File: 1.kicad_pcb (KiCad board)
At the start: 2 copper layers, 88.9 x 48.3 mm, 44 parts, among them J1 Micro_SD_Card, J10 I2C1, J11 I2C2, J12 B3..9A, J2 USB_B_Micro, J3 Conn_Power, J4 SWD, J5 Protected, J6 SPI1, J7 ADC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

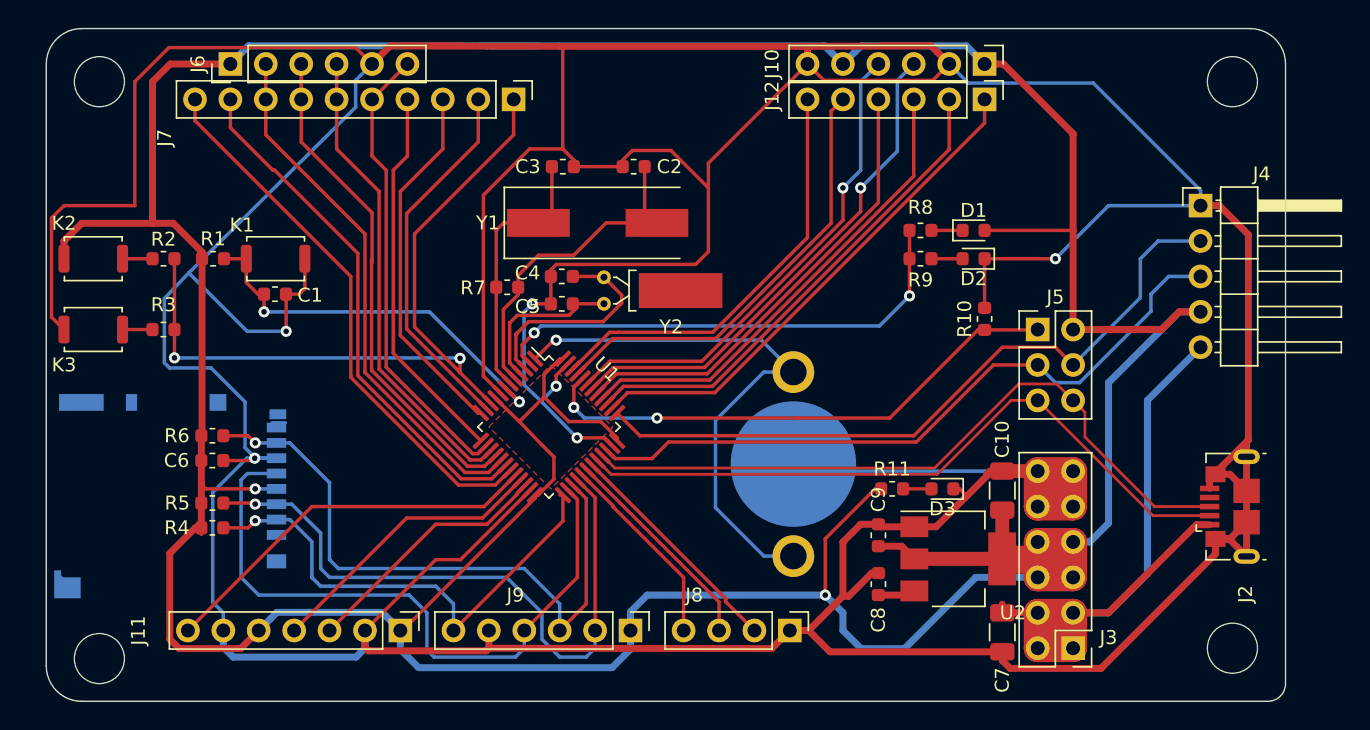
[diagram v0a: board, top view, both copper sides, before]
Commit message: move U1(STM32 Chip)
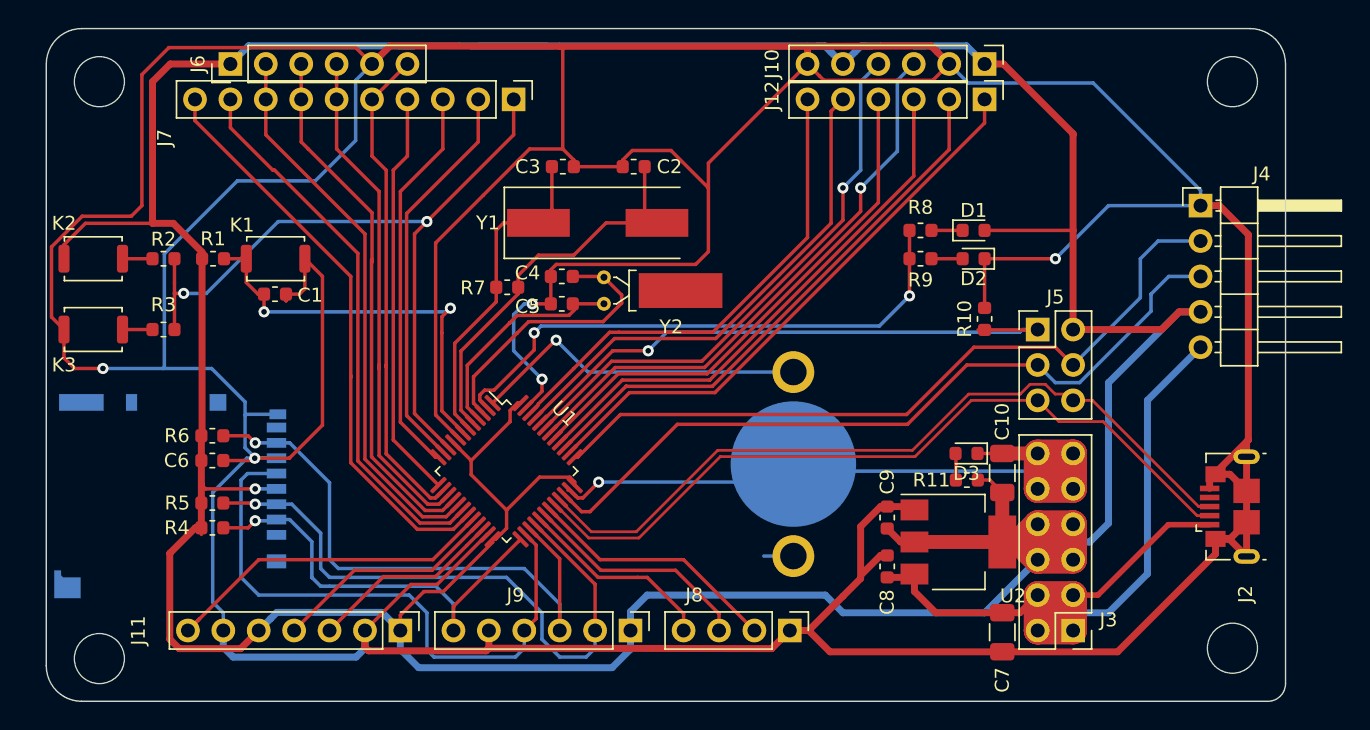
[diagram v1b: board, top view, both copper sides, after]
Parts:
- moved R11 5.40 mm to (162.6, 118.7), turned to 180 degrees
- moved U1 4.40 mm to (129.5, 118.1)
- moved D3 3.07 mm to (162.5, 116.8)
- moved C8 1.42 mm to (156.8, 124.9)
- moved C9 1.42 mm to (156.8, 121.4)
- moved J3 1.27 mm to (170.2, 129.5)
- moved C10 1.26 mm to (165.1, 118.2)
- moved U2 1.21 mm to (161.9, 123.2)
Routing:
- net GND: track 506.2 -> 528.3 mm
- net Net-(BT1-Pad1): track 40.3 -> 26.7 mm
- net +3V3: track 329.4 -> 316.5 mm, vias 2 -> 1
- net +5V: track 57.3 -> 63.4 mm
- net /USB_D-: track 50.0 -> 55.5 mm
- net /SD_SCLK: track 48.2 -> 43.1 mm
- net /RG_LED: track 35.6 -> 40.4 mm
- net /SWDIO: track 50.0 -> 54.8 mm
- net /SD_CS: track 37.3 -> 32.6 mm
- net /USB_D+: track 51.2 -> 55.6 mm
- net /OSC_8M1: track 24.1 -> 28.5 mm
- net /PB3: track 36.9 -> 41.4 mm
- net /PB9: track 30.6 -> 35.0 mm
- net /OSC_32K1: track 15.9 -> 20.3 mm
- net /PB11: track 18.4 -> 14.0 mm
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- removed copper zone on F.Cu, net +3V3

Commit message: move edge
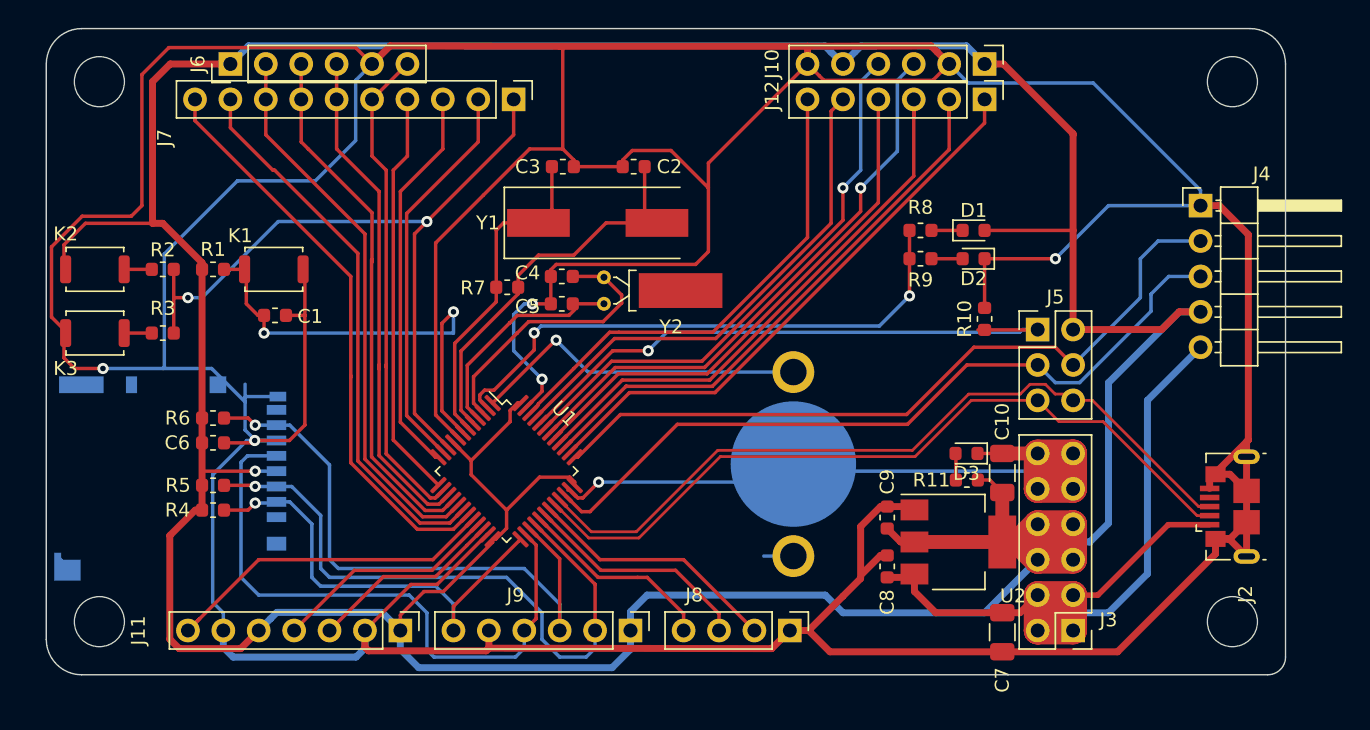
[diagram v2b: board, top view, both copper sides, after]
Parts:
- moved C1 1.52 mm to (112.9, 106.9)
- moved R4 1.27 mm to (108.5, 120.9)
- moved C6 1.27 mm to (108.5, 116.1)
- moved R5 1.27 mm to (108.5, 119.1)
- moved R6 1.27 mm to (108.5, 114.3)
- moved J1 1.27 mm to (105.4, 118.6)
- moved K1 0.77 mm to (112.8, 103.6)
- moved K2 0.77 mm to (100.0, 103.6)
- moved R2 0.76 mm to (104.9, 103.6)
- moved R1 0.76 mm to (108.5, 103.6)
- moved K3 0.28 mm to (100.0, 108.2)
- moved R3 0.26 mm to (104.9, 108.2)
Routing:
- net GND: track 528.3 -> 525.5 mm
- net +3V3: track 316.5 -> 315.1 mm
- net /NRST: track 29.5 -> 30.8 mm
- net /SD_SCLK: track 43.1 -> 44.3 mm
- net /SD_DO: track 42.4 -> 43.7 mm
- net /SD_DI: track 45.2 -> 46.4 mm
- net /SD_CS: track 32.6 -> 33.8 mm
- net /PA0: track 55.8 -> 55.0 mm
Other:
- board size 88.9 x 48.3 mm -> 88.9 x 46.4 mm
- board text added: "ADC CH9..0"
- board text added: "SWD"
- board text added: "USB"

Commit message: movdify some line
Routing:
- net /NRST: track 30.8 -> 30.1 mm
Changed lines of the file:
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@@
     (thickness 1.6)
     (drawings 27)
-    (tracks 664)
+    (tracks 665)
     (zones 0)
     (modules 44)
@@
   (segment (start 110.998 120.904) (end 111.506 120.396) (width 0.25) (layer F.Cu) (net 4))
   (segment (start 109.271 120.904) (end 110.998 120.904) (width 0.25) (layer F.Cu) (net 4))
-  (segment (start 112.141 108.204) (end 112.141 108.204) (width 0.25) (layer F.Cu) (net 5))
-  (via (at 125.73 106.68) (size 0.8) (drill 0.4) (layers F.Cu B.Cu) (net 5))
-  (segment (start 112.141 108.204) (end 112.141 108.204) (width 0.25) (layer F.Cu) (net 5))
-  (via (at 112.141 108.204) (size 0.8) (drill 0.4) (layers F.Cu B.Cu) (net 5))
-  (segment (start 126.419891 115.308103) (end 126.419891 115.343445) (width 0.25) (layer F.Cu) (net 5))
-  (segment (start 124.900666 113.788878) (end 126.419891 115.308103) (width 0.25) (layer F.Cu) (net 5))
-  (segment (start 125.73 106.68) (end 124.900666 107.509334) (width 0.25) (layer F.Cu) (net 5))
-  (segment (start 124.900666 107.509334) (end 124.900666 113.788878) (width 0.25) (layer F.Cu) (net 5))
-  (segment (start 112.141 108.204) (end 125.73 108.204) (width 0.25) (layer B.Cu) (net 5))
-  (segment (start 112.141 106.934) (end 112.141 108.204) (width 0.25) (layer F.Cu) (net 5))
   (segment (start 111.7035 106.934) (end 112.141 106.934) (width 0.25) (layer F.Cu) (net 5))
+  (segment (start 110.871 106.1015) (end 110.871 106.1015) (width 0.25) (layer F.Cu) (net 5))
+  (segment (start 110.871 104.394) (end 110.871 106.1015) (width 0.25) (layer F.Cu) (net 5))
+  (segment (start 109.271 103.632) (end 110.744 103.632) (width 0.25) (layer F.Cu) (net 5))
   (segment (start 110.871 106.1015) (end 111.7035 106.934) (width 0.25) (layer F.Cu) (net 5))
-  (segment (start 110.871 104.394) (end 110.871 106.1015) (width 0.25) (layer F.Cu) (net 5))
-  (segment (start 125.73 106.68) (end 125.73 108.204) (width 0.25) (layer B.Cu) (net 5))
-  (segment (start 109.271 103.632) (end 110.744 103.632) (width 0.25) (layer F.Cu) (net 5))
+  (via (at 110.871 106.1015) (size 0.8) (drill 0.4) (layers F.Cu B.Cu) (net 5))
+  (segment (start 110.871 106.1015) (end 125.4055 106.1015) (width 0.25) (layer B.Cu) (net 5))
+  (segment (start 125.4055 106.1015) (end 125.9135 106.1015) (width 0.25) (layer B.Cu) (net 5))
+  (segment (start 125.9135 106.1015) (end 125.9135 106.1015) (width 0.25) (layer B.Cu) (net 5))
+  (via (at 125.9135 106.1015) (size 0.8) (drill 0.4) (layers F.Cu B.Cu) (net 5))
+  (segment (start 124.900666 107.114334) (end 125.9135 106.1015) (width 0.25) (layer F.Cu) (net 5))
+  (segment (start 124.900666 113.788878) (end 124.900666 107.114334) (width 0.25) (layer F.Cu) (net 5))
+  (segment (start 126.419891 115.308103) (end 124.900666 113.788878) (width 0.25) (layer F.Cu) (net 5))
+  (segment (start 126.419891 115.343445) (end 126.419891 115.308103) (width 0.25) (layer F.Cu) (net 5))
   (segment (start 133.934717 119.469322) (end 133.970057 119.469322) (width 0.25) (layer F.Cu) (net 7))
   (segment (start 132.863822 104.194178) (end 132.8545 104.2035) (width 0.25) (layer F.Cu) (net 7))
@@
   (segment (start 170.18 93.9) (end 170.18 93.98) (width 0.5) (layer F.Cu) (net 8))
   (segment (start 163.83 88.9) (end 165.18 88.9) (width 0.5) (layer F.Cu) (net 8))
-  (segment (start 111.506 118.11) (end 107.95 118.11) (width 0.25) (layer F.Cu) (net 8))
   (segment (start 109.728 88.9) (end 105.41 88.9) (width 0.5) (layer F.Cu) (net 8))
   (segment (start 105.41 88.9) (end 104.14 90.17) (width 0.5) (layer F.Cu) (net 8))
@@
   (segment (start 99.33 100.33) (end 104.14 100.33) (width 0.25) (layer F.Cu) (net 8))
   (segment (start 97.79 101.87) (end 99.33 100.33) (width 0.25) (layer F.Cu) (net 8))
-  (segment (start 107.696 120.904) (end 107.696 116.078) (width 0.5) (layer F.Cu) (net 8))
   (segment (start 107.696 116.078) (end 107.696 114.3) (width 0.5) (layer F.Cu) (net 8))
   (segment (start 107.696 103.632) (end 107.696 114.3) (width 0.5) (layer F.Cu) (net 8))
@@
   (segment (start 107.696 103.157) (end 104.869 100.33) (width 0.5) (layer F.Cu) (net 8))
   (segment (start 107.696 103.632) (end 107.696 103.157) (width 0.5) (layer F.Cu) (net 8))
+  (segment (start 107.95 118.11) (end 107.696 117.856) (width 0.25) (layer F.Cu) (net 8))
+  (segment (start 111.506 118.11) (end 107.95 118.11) (width 0.25) (layer F.Cu) (net 8))
+  (segment (start 107.696 117.856) (end 107.696 116.078) (width 0.5) (layer F.Cu) (net 8))
+  (segment (start 107.696 120.904) (end 107.696 117.856) (width 0.5) (layer F.Cu) (net 8))
   (segment (start 170.25 129.64) (end 170.18 129.71) (width 0.25) (layer F.Cu) (net 10))
   (segment (start 179.324 109.22) (end 175.514 113.03) (width 0.5) (layer B.Cu) (net 10))

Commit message: gnd line
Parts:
- moved R7 0.82 mm to (128.8, 105.2)
- moved Y2 0.80 mm to (135.7, 106.1)
- moved C4 0.69 mm to (132.8, 104.1)
- moved C5 0.69 mm to (132.8, 106.1)
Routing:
- net GND: track 525.5 -> 545.1 mm
- net /OSC_32K2: track 16.1 -> 15.2 mm
- net /OSC_8M2: track 23.5 -> 24.3 mm
- net /RG_LED: track 40.4 -> 39.6 mm
- net /OSC_32K1: track 20.3 -> 19.8 mm

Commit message: op lines
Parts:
- moved J4 3.81 mm to (175.5, 99.1)
- moved J2 3.81 mm to (177.6, 120.7)
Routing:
- net +3V3: track 315.4 -> 289.7 mm
- net GND: track 545.1 -> 526.4 mm
- net +5V: track 63.4 -> 57.4 mm
- net /SWDCLK: track 54.0 -> 51.4 mm
- net /SWDIO: track 54.8 -> 52.7 mm
- net /USB_D+: track 55.6 -> 54.6 mm
- net /USB_D-: track 55.5 -> 54.9 mm
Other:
- board size 88.9 x 46.4 mm -> 86.4 x 46.4 mm

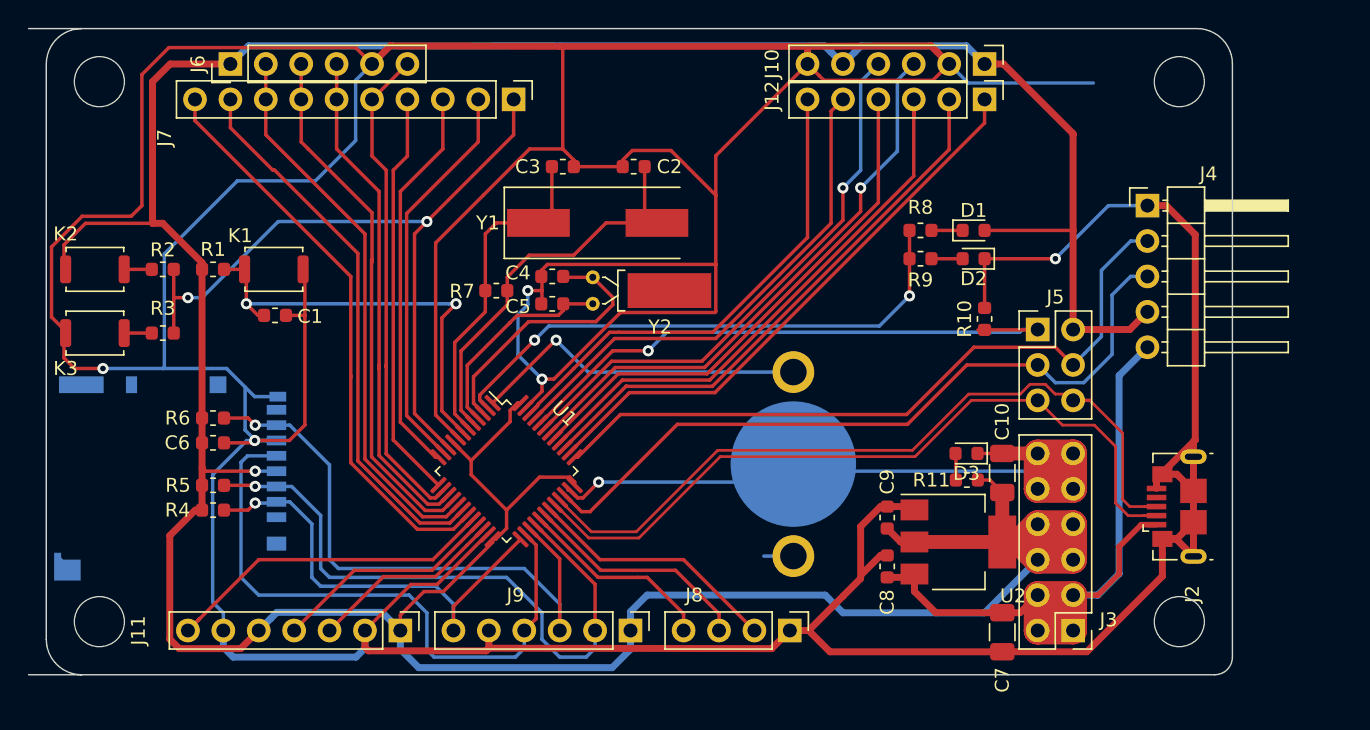
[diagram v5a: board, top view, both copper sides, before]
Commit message: resize edge
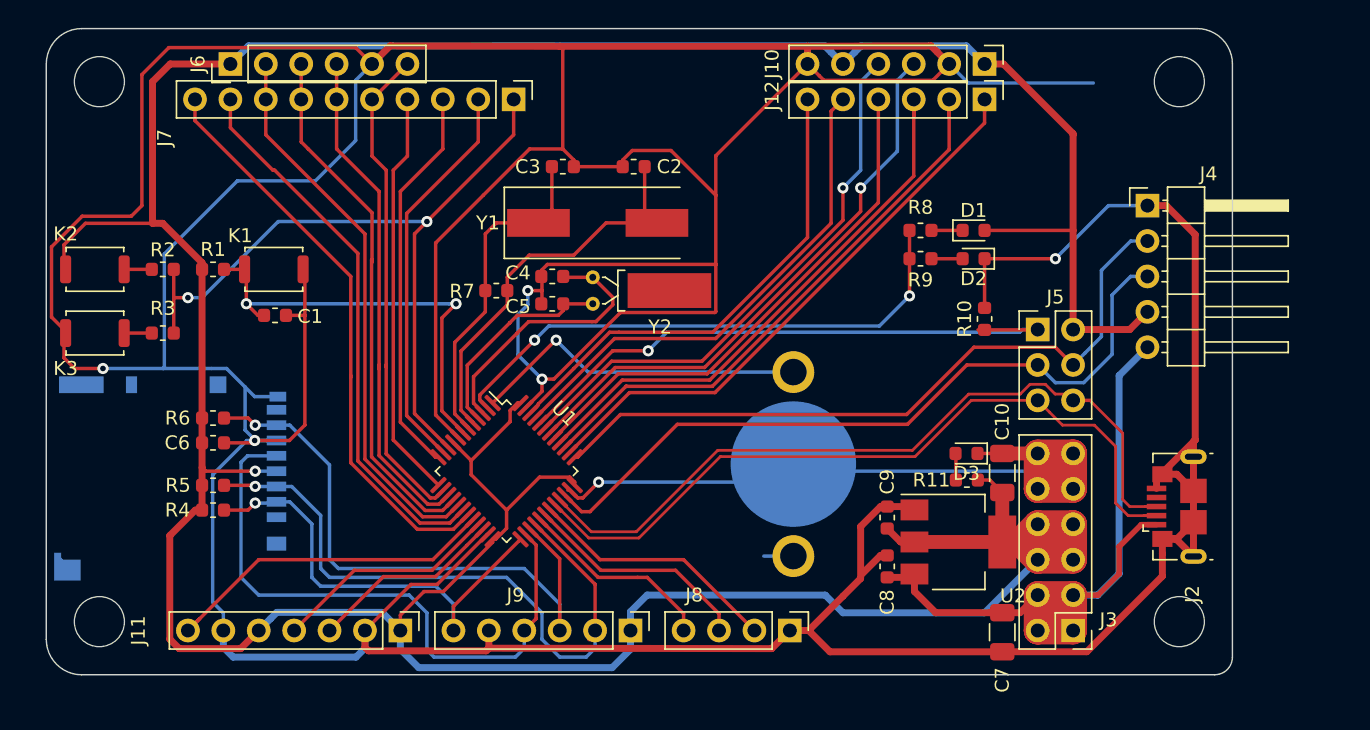
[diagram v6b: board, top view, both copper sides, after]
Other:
- board size 86.4 x 46.4 mm -> 85.1 x 46.4 mm
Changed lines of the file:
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@@
   (gr_arc (start 99.06 88.9) (end 99.06 86.36) (angle -90) (layer Edge.Cuts) (width 0.1))
   (gr_line (start 181.61 88.9) (end 181.61 131.445) (layer Edge.Cuts) (width 0.1))
-  (gr_line (start 95.25 86.36) (end 179.07 86.36) (layer Edge.Cuts) (width 0.1))
+  (gr_line (start 99.06 86.36) (end 179.07 86.36) (layer Edge.Cuts) (width 0.1))
   (gr_line (start 96.52 130.175) (end 96.52 88.9) (layer Edge.Cuts) (width 0.1))
-  (gr_line (start 180.34 132.715) (end 95.25 132.715) (layer Edge.Cuts) (width 0.1))
+  (gr_line (start 180.34 132.715) (end 99.06 132.715) (layer Edge.Cuts) (width 0.1))
   (gr_text "MCO Tx Rx GND" (at 146.05 132.08) (layer Dwgs.User)
     (effects (font (size 0.9 0.9) (thickness 0.15)))

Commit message: op gnd line
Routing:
- net GND: track 526.4 -> 535.6 mm
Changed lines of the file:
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@@
     (thickness 1.6)
     (drawings 27)
-    (tracks 672)
+    (tracks 674)
     (zones 0)
     (modules 44)
@@
   (segment (start 165.1 131.064) (end 171.166002 131.064) (width 0.5) (layer F.Cu) (net 7))
   (segment (start 172.72 99.06) (end 175.514 99.06) (width 0.25) (layer B.Cu) (net 7))
+  (segment (start 172.72 91.356) (end 171.628999 90.264999) (width 0.25) (layer B.Cu) (net 7))
+  (segment (start 172.72 99.06) (end 172.72 91.356) (width 0.25) (layer B.Cu) (net 7))
   (segment (start 163.83 100.838) (end 170.18 100.838) (width 0.25) (layer F.Cu) (net 8))
   (segment (start 170.18 100.838) (end 170.18 107.95) (width 0.5) (layer F.Cu) (net 8))
